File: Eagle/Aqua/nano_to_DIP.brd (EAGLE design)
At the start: 32.7 x 49.5 mm, 2 parts, among them IC1 ATMEGA168PROUND

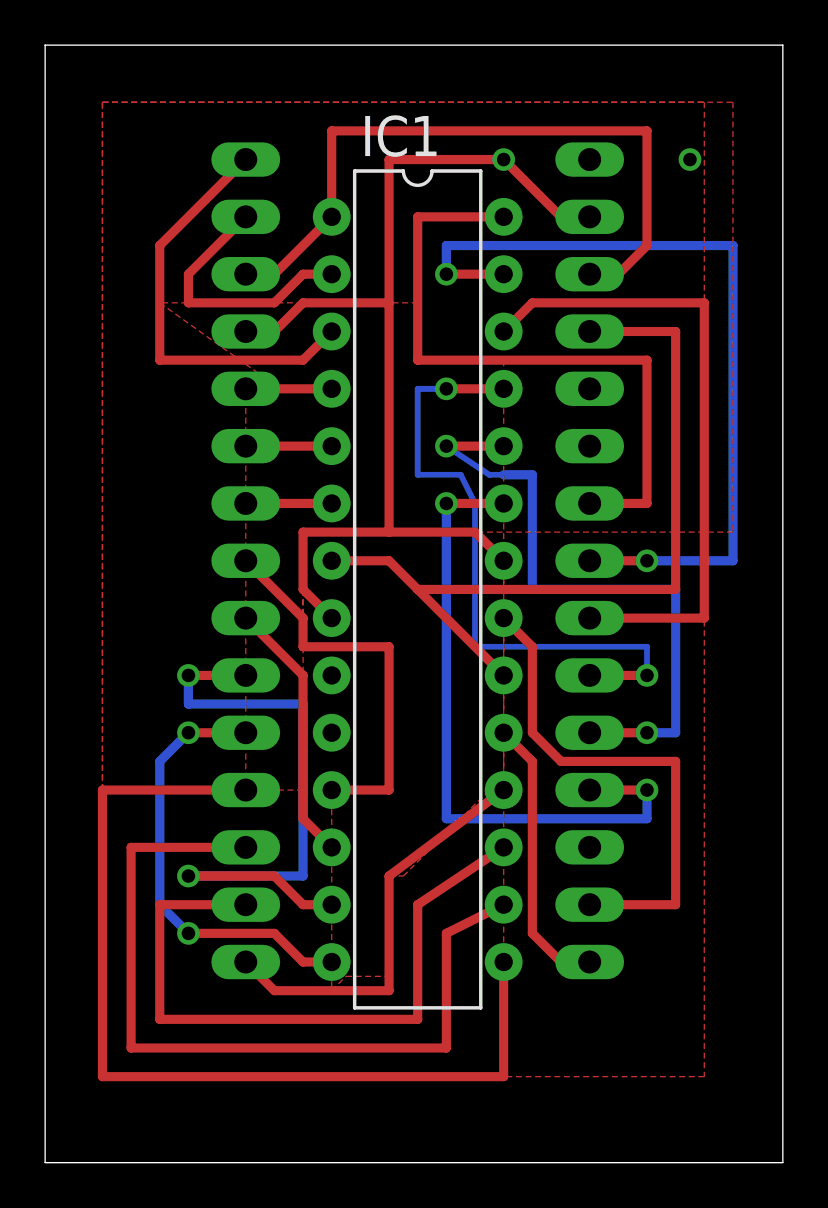
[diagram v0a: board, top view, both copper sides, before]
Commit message: Big update Many important fixes dictated by 1st prototype
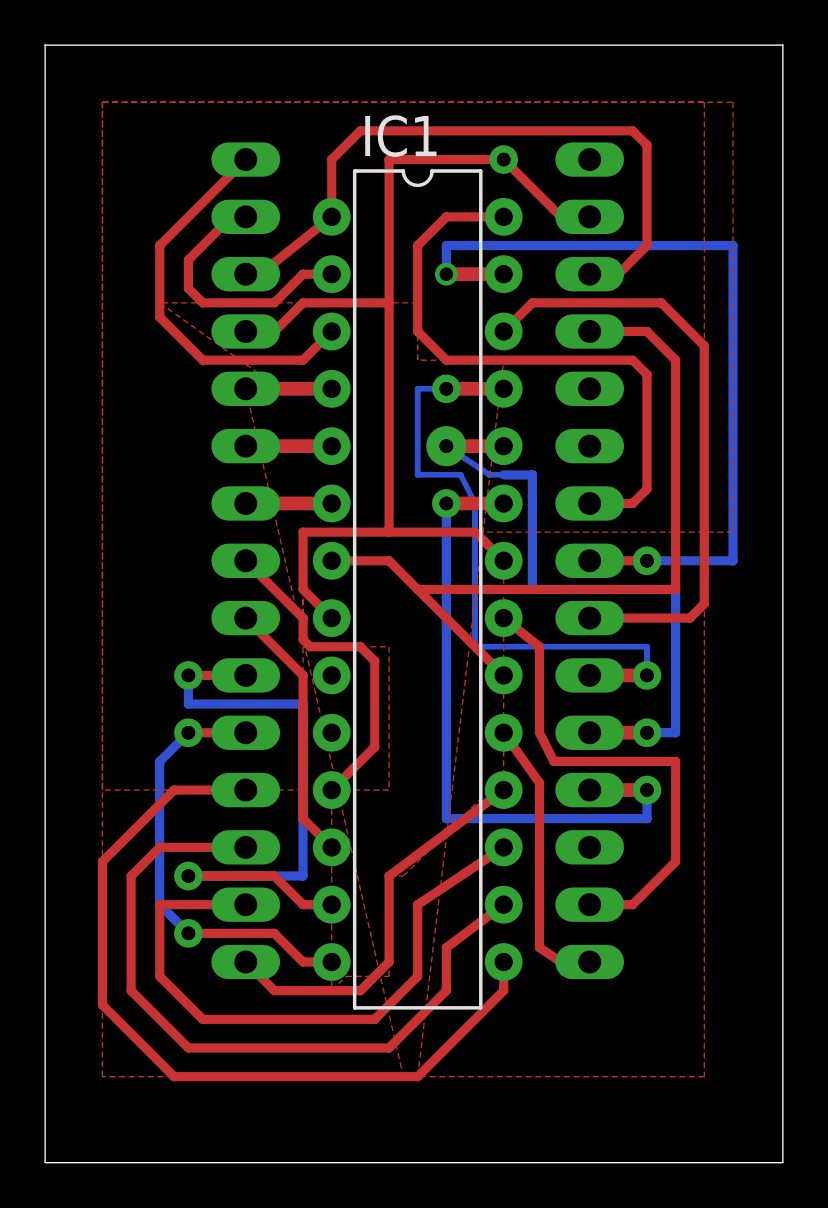
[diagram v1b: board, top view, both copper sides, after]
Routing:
- net N$22: track 41.9 -> 36.0 mm
- net N$11: track 35.9 -> 31.8 mm
- net N$19: track 17.6 -> 14.6 mm
- net N$17: track 29.2 -> 27.0 mm
- net N$10: track 30.0 -> 27.7 mm
- net N$15: track 28.5 -> 27.0 mm
- net N$3: track 30.8 -> 29.5 mm
- net N$1: track 18.6 -> 17.5 mm
- net N$24: track 22.6 -> 21.7 mm
- net N$7: track 18.3 -> 17.6 mm
- net N$5: track 36.4 -> 35.7 mm
- net N$6: vias 1 -> 2
- net N$23: vias 2 -> 4
- net N$21: vias 2 -> 4
- net N$16: vias 2 -> 3
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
